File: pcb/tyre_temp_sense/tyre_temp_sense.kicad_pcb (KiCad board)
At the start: 2 copper layers, 50 x 65 mm, 47 parts, among them J1 POWER & CAN, J2 5V, J3 Analog, J4 MUX Port 0, J5 MUX Port 1, J6 MUX Port 2, J7 MUX Port 3, J8 Conn_01x02, J9 GND, U1 TCA9548APWR, U2 MCP2515-I/ST, U3 MCP2551-I-SN, Y1 8 mhz

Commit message: revision 2
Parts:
- removed ? (x2): , 
- removed J9: GND, Connector_PinHeader_2.54mm:PinHeader_1x04_P2.54mm_Vertical
- removed the REF** at (116.0, 101.0)
- removed the REF** at (116.0, 44.0)
- removed the REF** at (74.0, 44.0)
- removed the REF** at (74.0, 101.0)
- added REF**: MountingHole_3.2mm_M3, MountingHole:MountingHole_3.2mm_M3, F.Cu at (69.0, 102.0)
- added REF**: MountingHole_3.2mm_M3, MountingHole:MountingHole_3.2mm_M3, F.Cu at (245.0, 102.0)
- added REF**: MountingHole_3.2mm_M3, MountingHole:MountingHole_3.2mm_M3, F.Cu at (245.0, 49.5)
- added REF**: MountingHole_3.2mm_M3, MountingHole:MountingHole_3.2mm_M3, F.Cu at (69.0, 49.5)
- C4: value 10uF -> 0.1uF
- J2: value 5V -> Extra i2c ports (no pullups); footprint Connector_PinHeader_2.54mm:PinHeader_1x04_P2.54mm_Vertical -> Connector_JST:JST_EH_B8B-EH-A_1x08_P2.50mm_Vertical
- J3: value Analog -> Analog breakout; footprint Connector_PinHeader_2.54mm:PinHeader_1x04_P2.54mm_Vertical -> Connector_JST:JST_EH_B4B-EH-A_1x04_P2.50mm_Vertical
- R1, R12: value 10k -> 10K
- R10, R11, R2, R3, R4, R5, R6, R7, R8, R9: value 4.7k -> 4.7K
- TP1: value CAN+ -> CAN_H
- TP3: value CAN- -> CAN_L
- Y1: footprint Crystal:Crystal_SMD_5032-2Pin_5.0x3.2mm -> Crystal:Crystal_SMD_3225-4Pin_3.2x2.5mm
- moved R2 140.3 mm to (232.0, 112.5), turned to 0 degrees
- moved U3 138.6 mm to (234.5, 52.0)
- moved R13 136.5 mm to (235.2, 27.0), turned to 0 degrees
- moved C1 133.3 mm to (224.0, 99.5), turned to 0 degrees
- moved C2 132.9 mm to (221.5, 43.0), turned to 0 degrees
- moved C3 131.7 mm to (216.5, 43.0), turned to 0 degrees
- moved R11 131.5 mm to (230.7, 117.0), turned to 0 degrees
- moved U1 130.8 mm to (226.0, 84.0)
- moved R8 129.1 mm to (235.2, 116.0)
- moved Y1 128.6 mm to (215.1, 52.9)
- moved R3 128.5 mm to (218.0, 111.9), turned to 0 degrees
- moved J1 128.2 mm to (234.5, 60.5)
- moved C4 128.2 mm to (224.0, 60.0), turned to 0 degrees
- moved J7 128.0 mm to (234.5, 70.5)
- moved J6 127.9 mm to (234.5, 78.0)
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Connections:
- net A0 renamed Net-(A1-Pad19)
- net A1 renamed Net-(A1-Pad20)
- net A2 renamed Net-(A1-Pad21)
- net A3 renamed Net-(A1-Pad22)
- J1 pad 3: CAN+ -> CAN_L
- J1 pad 4: CAN- -> CAN_H
- J2 pad 1: +5V -> Net-(J2-Pad1)
- J2 pad 2: +5V -> Net-(J2-Pad2)
- J2 pad 3: +5V -> Net-(J2-Pad3)
- J2 pad 4: +5V -> Net-(J2-Pad4)
- J4 pad 1: Net-(J4-Pad1) -> GND
- J4 pad 2: Net-(J4-Pad2) -> +3V3
- J4 pad 3: +3V3 -> Net-(J4-Pad3)
- J4 pad 4: GND -> Net-(J4-Pad4)
- J5 pad 1: Net-(J5-Pad1) -> GND
- J5 pad 2: Net-(J5-Pad2) -> +3V3
- J5 pad 3: +3V3 -> Net-(J5-Pad3)
- J5 pad 4: GND -> Net-(J5-Pad4)
- J6 pad 1: Net-(J6-Pad1) -> GND
- J6 pad 2: Net-(J6-Pad2) -> +3V3
- J6 pad 3: +3V3 -> Net-(J6-Pad3)
- J6 pad 4: GND -> Net-(J6-Pad4)
- J7 pad 1: Net-(J7-Pad1) -> GND
- J7 pad 2: Net-(J7-Pad2) -> +3V3
- J7 pad 3: +3V3 -> Net-(J7-Pad3)
- J7 pad 4: GND -> Net-(J7-Pad4)
- J8 pad 2: CAN- -> CAN_L
- R10 pad 2: Net-(J7-Pad2) -> Net-(J7-Pad3)
- R11 pad 2: Net-(J7-Pad1) -> Net-(J7-Pad4)
- R14 pad 2: CAN+ -> CAN_H
- R4 pad 2: Net-(J4-Pad2) -> Net-(J4-Pad3)
- R5 pad 2: Net-(J4-Pad1) -> Net-(J4-Pad4)
- R6 pad 2: Net-(J5-Pad2) -> Net-(J5-Pad3)
- R7 pad 2: Net-(J5-Pad1) -> Net-(J5-Pad4)
- R8 pad 2: Net-(J6-Pad2) -> Net-(J6-Pad3)
- R9 pad 2: Net-(J6-Pad1) -> Net-(J6-Pad4)
- TP1 pad 1: CAN- -> CAN_H
- TP3 pad 1: CAN+ -> CAN_L
- U1 pad 10: Net-(J7-Pad1) -> Net-(J7-Pad4)
- U1 pad 11: Net-(J7-Pad2) -> Net-(J7-Pad3)
- U1 pad 13: Net-(U1-Pad13) -> Net-(J2-Pad1)
- U1 pad 14: Net-(U1-Pad14) -> Net-(J2-Pad2)
- U1 pad 15: Net-(U1-Pad15) -> Net-(J2-Pad3)
- U1 pad 16: Net-(U1-Pad16) -> Net-(J2-Pad4)
- U1 pad 17: Net-(U1-Pad17) -> Net-(J2-Pad5)
- U1 pad 18: Net-(U1-Pad18) -> Net-(J2-Pad6)
- U1 pad 19: Net-(U1-Pad19) -> Net-(J2-Pad7)
- U1 pad 20: Net-(U1-Pad20) -> Net-(J2-Pad8)
- U1 pad 4: Net-(J4-Pad1) -> Net-(J4-Pad4)
- U1 pad 5: Net-(J4-Pad2) -> Net-(J4-Pad3)
- U1 pad 6: Net-(J5-Pad1) -> Net-(J5-Pad4)
- U1 pad 7: Net-(J5-Pad2) -> Net-(J5-Pad3)
- U1 pad 8: Net-(J6-Pad1) -> Net-(J6-Pad4)
- U1 pad 9: Net-(J6-Pad2) -> Net-(J6-Pad3)
- U3 pad 6: CAN- -> CAN_L
- U3 pad 7: CAN+ -> CAN_H
- Y1 pad 1: Net-(C3-Pad1) -> Net-(C2-Pad1)
- Y1 pad 2: Net-(C2-Pad1) -> Net-(C3-Pad1)
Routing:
- net +5V: track 246.6 -> 0.00 mm, vias 5 -> 0
- net MOSI_CAN: track 76.1 -> 0.00 mm, vias 1 -> 0
- net MISO_CAN: track 69.6 -> 0.00 mm, vias 1 -> 0
- net CLK_CAN: track 63.8 -> 0.00 mm, vias 1 -> 0
- net +3V3: track 52.6 -> 0.00 mm
- net D6: track 50.2 -> 0.00 mm, vias 1 -> 0
- net D2: track 45.7 -> 0.00 mm, vias 1 -> 0
- net CAN-: track 36.2 -> 0.00 mm, vias 1 -> 0
- net Net-(J4-Pad2): track 33.7 -> 0.00 mm
- net CAN+: track 32.7 -> 0.00 mm, vias 2 -> 0
- net Net-(J4-Pad1): track 30.7 -> 0.00 mm
- net GND: track 27.6 -> 0.00 mm, vias 29 -> 0
- net Net-(J5-Pad2): track 25.2 -> 0.00 mm
- net Net-(J5-Pad1): track 22.5 -> 0.00 mm
- net Net-(A1-Pad19): track 21.4 -> 0.00 mm
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- removed copper zone on B.Cu, net GND
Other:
- board size 50 x 65 mm -> 184 x 60.5 mm
- board text removed: "120Ω"
- board text removed: "5V"
- board text removed: "A0"
- board text removed: "A1"
- board text removed: "A2"
- board text removed: "A3"
- board text removed: "AUMT 2021 Tyre Temp Bryce Chung"
- board text removed: "Arduino is wet Arduino is dry Arduino is warm"
- board text removed: "CANH"
- board text removed: "CANL"
- board text removed: "CLK"
- board text removed: "DATA CLK 3V3 GND"
- board text removed: "Debug Table Condition Issue"
- board text removed: "GND"
- board text removed: "JLCJLCJLCJLC"
- board text removed: "MISO"
- board text removed: "MOSI"
- board text removed: "RX"
- board text removed: "Raining Not raining Australia"
- board text removed: "TX"

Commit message: Second revision
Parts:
- removed the J2 at (210.0, 92.5)
- removed the J5 at (234.5, 85.5)
- removed the REF** at (69.0, 102.0)
- removed the REF** at (245.0, 102.0)
- removed the REF** at (245.0, 49.5)
- removed the REF** at (69.0, 49.5)
- removed TP1: CAN_H, TestPoint:TestPoint_Pad_D1.5mm
- removed TP2: GND, TestPoint:TestPoint_Pad_D1.5mm
- removed TP3: CAN_L, TestPoint:TestPoint_Pad_D1.5mm
- removed TP4: 5V, TestPoint:TestPoint_Pad_D1.5mm
- removed TP5: MOSI, TestPoint:TestPoint_Pad_D1.5mm
- removed TP6: MISO, TestPoint:TestPoint_Pad_D1.5mm
- removed TP7: CLK, TestPoint:TestPoint_Pad_D1.5mm
- added J6: Conn_01x02, Connector_PinHeader_2.54mm:PinHeader_1x02_P2.54mm_Vertical, F.Cu at (104.4, 73.3)
- added J7: A, Connector_PinHeader_2.54mm:PinHeader_1x04_P2.54mm_Vertical, F.Cu at (77.0, 70.5)
- added J9: GND, Connector_PinHeader_2.54mm:PinHeader_1x04_P2.54mm_Vertical, F.Cu at (77.0, 73.2)
- added REF**: MountingHole_3.2mm_M3, MountingHole:MountingHole_3.2mm_M3, F.Cu at (127.0, 57.5)
- added REF**: MountingHole_3.2mm_M3, MountingHole:MountingHole_3.2mm_M3, F.Cu at (60.0, 57.5)
- added REF**: MountingHole_3.2mm_M3, MountingHole:MountingHole_3.2mm_M3, F.Cu at (60.0, 91.0)
- added REF**: MountingHole_3.2mm_M3, MountingHole:MountingHole_3.2mm_M3, F.Cu at (127.0, 91.0)
- J3: value Analog breakout -> MUX Port 1
- J8: value Conn_01x02 -> GND; footprint Connector_PinHeader_2.54mm:PinHeader_1x02_P2.54mm_Vertical -> Connector_PinHeader_2.54mm:PinHeader_1x04_P2.54mm_Vertical
- R14: footprint Resistor_SMD:R_0603_1608Metric -> Resistor_SMD:R_1210_3225Metric
- Y1: footprint Crystal:Crystal_SMD_3225-4Pin_3.2x2.5mm -> Crystal:Crystal_SMD_5032-2Pin_5.0x3.2mm
- moved R11 165.0 mm to (77.3, 56.1), turned to 180 degrees
- moved R8 159.7 mm to (87.1, 56.3)
- moved R10 158.9 mm to (73.2, 56.1)
- moved J5 158.3 mm to (76.6, 60.2), turned to 180 degrees
- moved R9 146.8 mm to (91.2, 56.3), turned to 180 degrees
- moved J4 145.2 mm to (90.4, 60.2), turned to 180 degrees
- moved J8 143.5 mm to (77.0, 67.8), turned to 90 degrees
- moved R2 143.3 mm to (93.9, 74.0)
- moved R13 133.1 mm to (112.3, 78.2), turned to 270 degrees
- moved U1 133.1 mm to (93.8, 69.0), turned to 270 degrees
- moved R6 128.4 mm to (101.5, 56.3)
- moved C3 127.4 mm to (99.7, 71.9), turned to 180 degrees
- moved R4 126.7 mm to (115.3, 56.4)
- moved R3 125.8 mm to (98.1, 74.0), turned to 180 degrees
- moved R14 122.9 mm to (108.6, 73.5)
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- renumbered C2 to C1, C3 to C2, C1 to C3, J4 to J2, J6 to J4, J7 to J5
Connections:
- A1 pad 19: Net-(A1-Pad19) -> A0
- A1 pad 20: Net-(A1-Pad20) -> A1
- A1 pad 21: Net-(A1-Pad21) -> A2
- A1 pad 22: Net-(A1-Pad22) -> A3
- J1 pad 3: CAN_L -> CAN+
- J1 pad 4: CAN_H -> CAN-
- J2 pad 1: GND -> Net-(J2-Pad1)
- J2 pad 2: +3V3 -> Net-(J2-Pad2)
- J2 pad 3: Net-(J4-Pad3) -> GND
- J2 pad 4: Net-(J4-Pad4) -> +3V3
- J3 pad 1: Net-(A1-Pad22) -> Net-(J3-Pad1)
- J3 pad 2: Net-(A1-Pad21) -> Net-(J3-Pad2)
- J3 pad 3: Net-(A1-Pad20) -> GND
- J3 pad 4: Net-(A1-Pad19) -> +3V3
- J4 pad 1: GND -> Net-(J4-Pad1)
- J4 pad 2: +3V3 -> Net-(J4-Pad2)
- J4 pad 3: Net-(J6-Pad3) -> GND
- J4 pad 4: Net-(J6-Pad4) -> +3V3
- J5 pad 1: GND -> Net-(J5-Pad1)
- J5 pad 2: +3V3 -> Net-(J5-Pad2)
- J5 pad 3: Net-(J7-Pad3) -> GND
- J5 pad 4: Net-(J7-Pad4) -> +3V3
- J8 pad 1: Net-(J8-Pad1) -> GND
- J8 pad 2: CAN_L -> GND
- R10 pad 2: Net-(J7-Pad3) -> Net-(J5-Pad2)
- R11 pad 2: Net-(J7-Pad4) -> Net-(J5-Pad1)
- R14 pad 1: Net-(J8-Pad1) -> Net-(J6-Pad1)
- R14 pad 2: CAN_H -> CAN+
- R4 pad 2: Net-(J4-Pad3) -> Net-(J2-Pad2)
- R5 pad 2: Net-(J4-Pad4) -> Net-(J2-Pad1)
- R6 pad 2: Net-(J5-Pad3) -> Net-(J3-Pad2)
- R7 pad 2: Net-(J5-Pad4) -> Net-(J3-Pad1)
- R8 pad 2: Net-(J6-Pad3) -> Net-(J4-Pad2)
- R9 pad 2: Net-(J6-Pad4) -> Net-(J4-Pad1)
- U1 pad 10: Net-(J7-Pad4) -> Net-(J5-Pad1)
- U1 pad 11: Net-(J7-Pad3) -> Net-(J5-Pad2)
- U1 pad 4: Net-(J4-Pad4) -> Net-(J2-Pad1)
- U1 pad 5: Net-(J4-Pad3) -> Net-(J2-Pad2)
- U1 pad 6: Net-(J5-Pad4) -> Net-(J3-Pad1)
- U1 pad 7: Net-(J5-Pad3) -> Net-(J3-Pad2)
- U1 pad 8: Net-(J6-Pad4) -> Net-(J4-Pad1)
- U1 pad 9: Net-(J6-Pad3) -> Net-(J4-Pad2)
- U3 pad 6: CAN_L -> CAN-
- U3 pad 7: CAN_H -> CAN+
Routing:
- net +5V: track 0.00 -> 169.7 mm
- net +3V3: track 0.00 -> 106.0 mm
- net D2: track 0.00 -> 47.1 mm
- net Net-(J2-Pad1): track 0.00 -> 31.5 mm
- net D6: track 0.00 -> 30.7 mm
- net Net-(J2-Pad2): track 0.00 -> 29.0 mm
- net Net-(J5-Pad2): track 0.00 -> 23.7 mm
- net CAN-: track 0.00 -> 23.4 mm
- net GND: track 0.00 -> 23.1 mm, vias 0 -> 14
- net Net-(J5-Pad1): track 0.00 -> 22.1 mm
- net Net-(U2-Pad2): track 0.00 -> 21.6 mm
- net MOSI_CAN: track 0.00 -> 21.0 mm
- net CLK_CAN: track 0.00 -> 20.0 mm, vias 0 -> 2
- net Net-(J3-Pad1): track 0.00 -> 18.2 mm
- net Net-(U2-Pad1): track 0.00 -> 17.8 mm
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- added copper zone on B.Cu, net GND
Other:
- board size 184 x 60.5 mm -> 75 x 41.5 mm
- board text added: "120Ω Enable"
- board text added: "3v3 GND SCL SDA"
- board text added: "5V"
- board text added: "A3-A0"
- board text added: "AUMT 2021 - Bryce Chung Tyre Temperature Sensor Control Board Ultra 4000 +"
- board text added: "CAN & POWER"
- board text added: "CANL CANH 5V GND"
- board text added: "CANboos Zone"
- board text added: "GND"
- board text added: "JLCJLCJLCJLC"
- board text added: "MUX Port 0"
- board text added: "MUX Port 1"
- board text added: "MUX Port 2"
- board text added: "MUX Port 3"
- board text added: "RX"
- board text added: "TX"

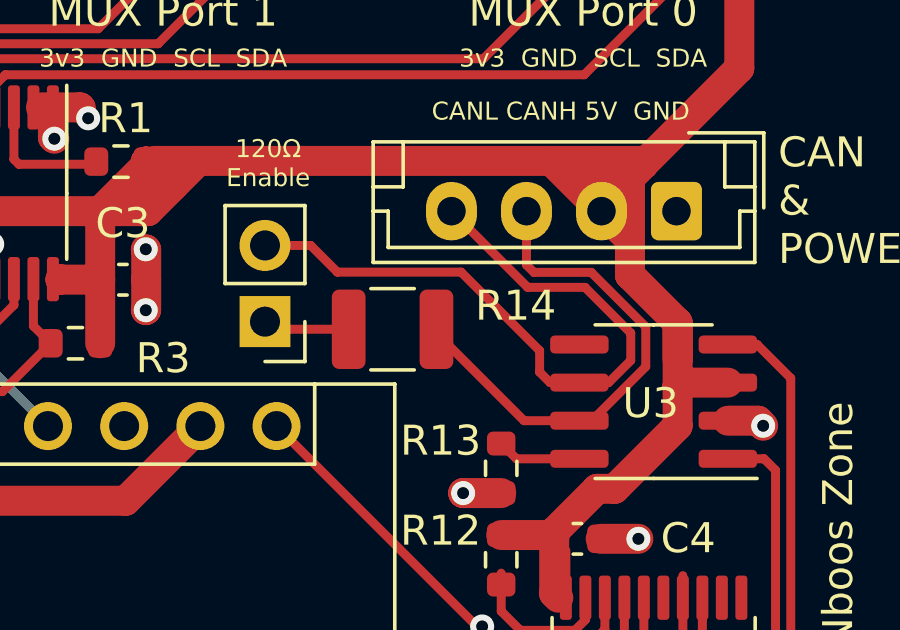
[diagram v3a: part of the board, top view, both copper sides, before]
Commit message: Added LCSC Part info
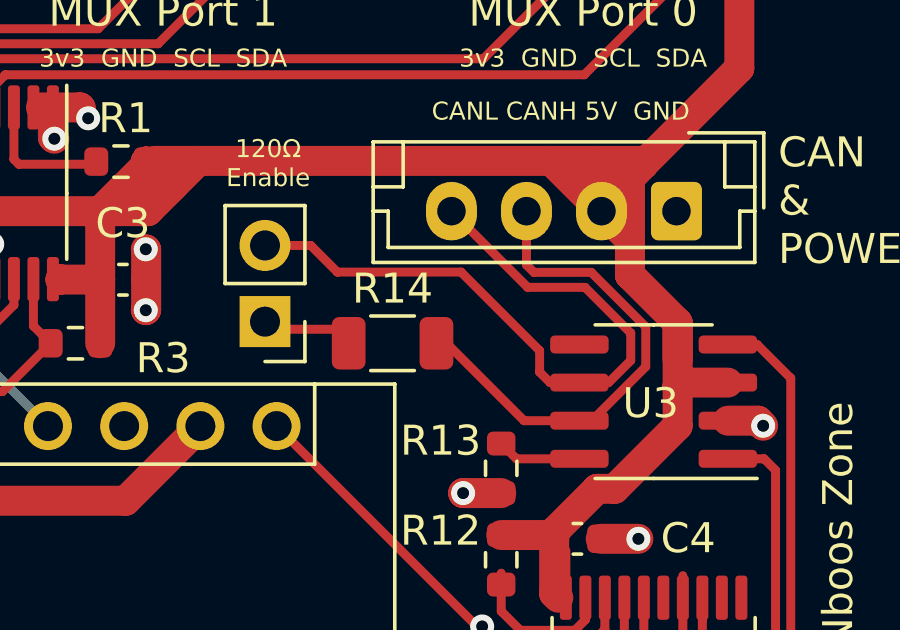
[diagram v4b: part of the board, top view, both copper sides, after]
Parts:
- C4: value 0.1uF -> 1uF
- R14: footprint Resistor_SMD:R_1210_3225Metric -> Resistor_SMD:R_1206_3216Metric
- moved R14 0.47 mm to (108.6, 74.0)
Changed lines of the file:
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@@
   )
   (setup
-    (last_trace_width 1)
+    (last_trace_width 0.25)
     (user_trace_width 0.3)
     (user_trace_width 1)
@@
     (add_net SDA)
   )
+  (module Resistor_SMD:R_1206_3216Metric (layer F.Cu)
+    (at 108.6465 74)
+    (descr "Resistor SMD 1206 (3216 Metric), square (rectangular) end terminal, IPC_7351 nominal, (Body size source: IPC-SM-782 page 72, https://www.pcb-3d.com/wordpress/wp-content/uploads/ipc-sm-782a_amendment_1_and_2.pdf), generated with kicad-footprint-generator")
+    (tags resistor)
+    (attr smd)
+    (fp_text reference R14 (at 0 -1.82) (layer F.SilkS)
+      (effects (font (size 1 1) (thickness 0.15)))
+    )
+    (fp_text value 120 (at 0 1.82) (layer F.Fab)
+      (effects (font (size 1 1) (thickness 0.15)))
+    )
+    (fp_line (start 2.28 1.12) (end -2.28 1.12) (layer F.CrtYd) (width 0.05))
+    (fp_line (start 2.28 -1.12) (end 2.28 1.12) (layer F.CrtYd) (width 0.05))
+    (fp_line (start -2.28 -1.12) (end 2.28 -1.12) (layer F.CrtYd) (width 0.05))
+    (fp_line (start -2.28 1.12) (end -2.28 -1.12) (layer F.CrtYd) (width 0.05))
+    (fp_line (start -0.727064 0.91) (end 0.727064 0.91) (layer F.SilkS) (width 0.12))
+    (fp_line (start -0.727064 -0.91) (end 0.727064 -0.91) (layer F.SilkS) (width 0.12))
+    (fp_line (start 1.6 0.8) (end -1.6 0.8) (layer F.Fab) (width 0.1))
+    (fp_line (start 1.6 -0.8) (end 1.6 0.8) (layer F.Fab) (width 0.1))
+    (fp_line (start -1.6 -0.8) (end 1.6 -0.8) (layer F.Fab) (width 0.1))
+    (fp_line (start -1.6 0.8) (end -1.6 -0.8) (layer F.Fab) (width 0.1))
+    (fp_text user %R (at 0 0) (layer F.Fab)
+      (effects (font (size 0.8 0.8) (thickness 0.12)))
+    )
+    (pad 2 smd roundrect (at 1.4625 0) (size 1.125 1.75) (layers F.Cu F.Paste F.Mask) (roundrect_rratio 0.222222)
+      (net 63 CAN+))
+    (pad 1 smd roundrect (at -1.4625 0) (size 1.125 1.75) (layers F.Cu F.Paste F.Mask) (roundrect_rratio 0.222222)
+      (net 46 "Net-(J6-Pad1)"))
+    (model ${KISYS3DMOD}/Resistor_SMD.3dshapes/R_1206_3216Metric.wrl
+      (at (xyz 0 0 0))
+      (scale (xyz 1 1 1))
+      (rotate (xyz 0 0 0))
+    )
+  )
   (module Connector_PinHeader_2.54mm:PinHeader_1x04_P2.54mm_Vertical (layer F.Cu)
     (at 77 67.75 90)
@@
       (effects (font (size 1 1) (thickness 0.15)))
     )
-    (fp_text user %R (at 0 -1.65) (layer F.Fab)
-      (effects (font (size 1 1) (thickness 0.15)))
-    )
     (fp_circle (center 0 0) (end 1.25 0) (layer F.CrtYd) (width 0.05))
     (fp_circle (center 0 0) (end 0 0.95) (layer F.SilkS) (width 0.12))
+    (fp_text user %R (at 0 -1.65) (layer F.Fab)
+      (effects (font (size 1 1) (thickness 0.15)))
+    )
     (pad 1 smd circle (at 0 0) (size 1.5 1.5) (layers F.Cu F.Mask)
       (net 25 "Net-(A1-Pad1)"))
@@
       (effects (font (size 1 1) (thickness 0.15)))
     )
-    (fp_text user %R (at 0 -1.65) (layer F.Fab)
-      (effects (font (size 1 1) (thickness 0.15)))
-    )
     (fp_circle (center 0 0) (end 1.25 0) (layer F.CrtYd) (width 0.05))
     (fp_circle (center 0 0) (end 0 0.95) (layer F.SilkS) (width 0.12))
+    (fp_text user %R (at 0 -1.65) (layer F.Fab)
+      (effects (font (size 1 1) (thickness 0.15)))
+    )
     (pad 1 smd circle (at 0 0) (size 1.5 1.5) (layers F.Cu F.Mask)
       (net 23 "Net-(A1-Pad2)"))
@@
     )
   )
-  (module Resistor_SMD:R_1210_3225Metric (layer F.Cu)
-    (at 108.6465 73.533)
-    (descr "Resistor SMD 1210 (3225 Metric), square (rectangular) end terminal, IPC_7351 nominal, (Body size source: IPC-SM-782 page 72, https://www.pcb-3d.com/wordpress/wp-content/uploads/ipc-sm-782a_amendment_1_and_2.pdf), generated with kicad-footprint-generator")
-    (tags resistor)
-    (attr smd)
-    (fp_text reference R14 (at 4.1035 -0.783) (layer F.SilkS)
-      (effects (font (size 1 1) (thickness 0.15)))
-    )
-    (fp_text value 120 (at 0 2.28) (layer F.Fab)
-      (effects (font (size 1 1) (thickness 0.15)))
-    )
-    (fp_text user %R (at 0 0) (layer F.Fab)
-      (effects (font (size 0.8 0.8) (thickness 0.12)))
-    )
-    (fp_line (start -1.6 1.245) (end -1.6 -1.245) (layer F.Fab) (width 0.1))
-    (fp_line (start -1.6 -1.245) (end 1.6 -1.245) (layer F.Fab) (width 0.1))
-    (fp_line (start 1.6 -1.245) (end 1.6 1.245) (layer F.Fab) (width 0.1))
-    (fp_line (start 1.6 1.245) (end -1.6 1.245) (layer F.Fab) (width 0.1))
-    (fp_line (start -0.723737 -1.355) (end 0.723737 -1.355) (layer F.SilkS) (width 0.12))
-    (fp_line (start -0.723737 1.355) (end 0.723737 1.355) (layer F.SilkS) (width 0.12))
-    (fp_line (start -2.28 1.58) (end -2.28 -1.58) (layer F.CrtYd) (width 0.05))
-    (fp_line (start -2.28 -1.58) (end 2.28 -1.58) (layer F.CrtYd) (width 0.05))
-    (fp_line (start 2.28 -1.58) (end 2.28 1.58) (layer F.CrtYd) (width 0.05))
-    (fp_line (start 2.28 1.58) (end -2.28 1.58) (layer F.CrtYd) (width 0.05))
-    (pad 2 smd roundrect (at 1.4625 0) (size 1.125 2.65) (layers F.Cu F.Paste F.Mask) (roundrect_rratio 0.222222)
-      (net 63 CAN+))
-    (pad 1 smd roundrect (at -1.4625 0) (size 1.125 2.65) (layers F.Cu F.Paste F.Mask) (roundrect_rratio 0.222222)
-      (net 46 "Net-(J6-Pad1)"))
-    (model ${KISYS3DMOD}/Resistor_SMD.3dshapes/R_1210_3225Metric.wrl
-      (at (xyz 0 0 0))
-      (scale (xyz 1 1 1))
-      (rotate (xyz 0 0 0))
-    )
-  )
   (module Capacitor_SMD:C_0603_1608Metric (layer F.Cu)
     (at 114.808 80.518)
@@
       (effects (font (size 1 1) (thickness 0.15)))
     )
-    (fp_text value 0.1uF (at 0 1.43) (layer F.Fab)
+    (fp_text value 1uF (at 0 1.43) (layer F.Fab)
       (effects (font (size 1 1) (thickness 0.15)))
     )
@@
     )
     (fp_text value "8 mhz" (at 0 2.8) (layer F.Fab)
-      (effects (font (size 1 1) (thickness 0.15)))
-    )
-    (fp_text user %R (at 0 0) (layer F.Fab)
       (effects (font (size 1 1) (thickness 0.15)))
     )
@@
     (fp_circle (center 0 0) (end 0.213333 0) (layer F.Adhes) (width 0.133333))
     (fp_circle (center 0 0) (end 0.093333 0) (layer F.Adhes) (width 0.186667))
+    (fp_text user %R (at 0 0) (layer F.Fab)
+      (effects (font (size 1 1) (thickness 0.15)))
+    )
     (pad 2 smd rect (at 1.85 0) (size 2 2.4) (layers F.Cu F.Paste F.Mask)
       (net 31 "Net-(C2-Pad1)"))
@@
       (effects (font (size 1 1) (thickness 0.15)))
     )
-    (fp_text user %R (at 0.3 0) (layer F.Fab)
-      (effects (font (size 1 1) (thickness 0.15)))
-    )
     (fp_circle (center 0 0) (end 3.2 0) (layer Cmts.User) (width 0.15))
     (fp_circle (center 0 0) (end 3.45 0) (layer F.CrtYd) (width 0.05))
+    (fp_text user %R (at 0.3 0) (layer F.Fab)
+      (effects (font (size 1 1) (thickness 0.15)))
+    )
     (pad 1 np_thru_hole circle (at 0 0) (size 3.2 3.2) (drill 3.2) (layers *.Cu *.Mask))
   )
@@
       (effects (font (size 1 1) (thickness 0.15)))
     )
-    (fp_text user %R (at 3.75 1.5) (layer F.Fab)
-      (effects (font (size 1 1) (thickness 0.15)))
-    )
     (fp_line (start -2.91 2.61) (end -0.41 2.61) (layer F.Fab) (width 0.1))
     (fp_line (start -2.91 0.11) (end -2.91 2.61) (layer F.Fab) (width 0.1))
@@
     (fp_line (start -2.5 2.2) (end 10 2.2) (layer F.Fab) (width 0.1))
     (fp_line (start -2.5 -1.6) (end -2.5 2.2) (layer F.Fab) (width 0.1))
+    (fp_text user %R (at 3.75 1.5) (layer F.Fab)
+      (effects (font (size 1 1) (thickness 0.15)))
+    )
     (pad 1 thru_hole roundrect (at 0 0 180) (size 1.7 1.95) (drill 0.95) (layers *.Cu *.Mask) (roundrect_rratio 0.147059)
       (net 56 "Net-(J2-Pad1)"))
@@
   (segment (start 119.823 76.581) (end 120.831 76.581) (width 1) (layer F.Cu) (net 5))
   (segment (start 97.325 66.1375) (end 96.92501 66.1375) (width 1) (layer F.Cu) (net 5))
-  (segment (start 112.268 81.662) (end 112.268 81.788) (width 0.3) (layer F.Cu) (net 27))
   (segment (start 114.423 82.4815) (end 114.423 80.908) (width 0.3) (layer F.Cu) (net 9))
   (segment (start 118.14799 73.312776) (end 118.14799 74.543088) (width 1) (layer F.Cu) (net 9))
@@
   (segment (start 96.025 67.868) (end 96.025 66.1375) (width 0.3) (layer F.Cu) (net 26))
   (segment (start 96.190008 68.033008) (end 96.025 67.868) (width 0.3) (layer F.Cu) (net 26))
+  (segment (start 112.268 81.662) (end 112.268 81.788) (width 0.3) (layer F.Cu) (net 27))
   (segment (start 115.073 83.219) (end 115.073 82.4815) (width 0.3) (layer F.Cu) (net 27))
   (segment (start 114.72299 83.56901) (end 112.90601 83.56901) (width 0.3) (layer F.Cu) (net 27))
